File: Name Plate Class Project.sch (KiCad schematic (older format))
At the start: 0 parts

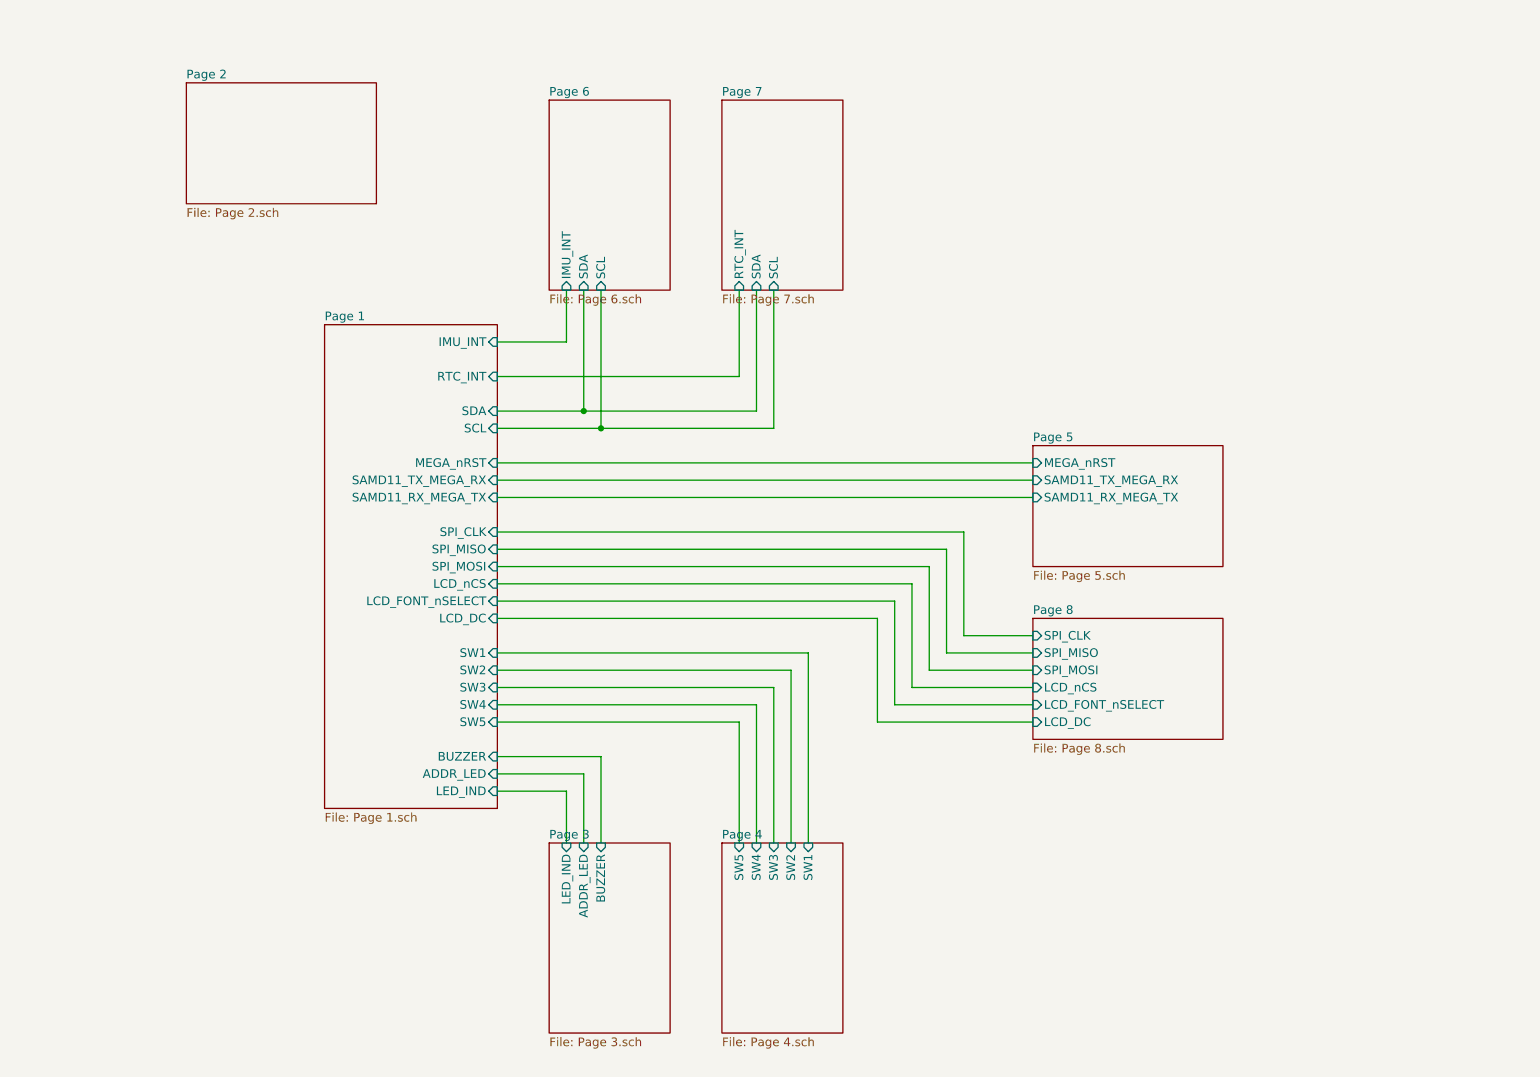
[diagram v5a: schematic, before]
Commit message: Updates to schematic
Switching to ATMega34UF chip.
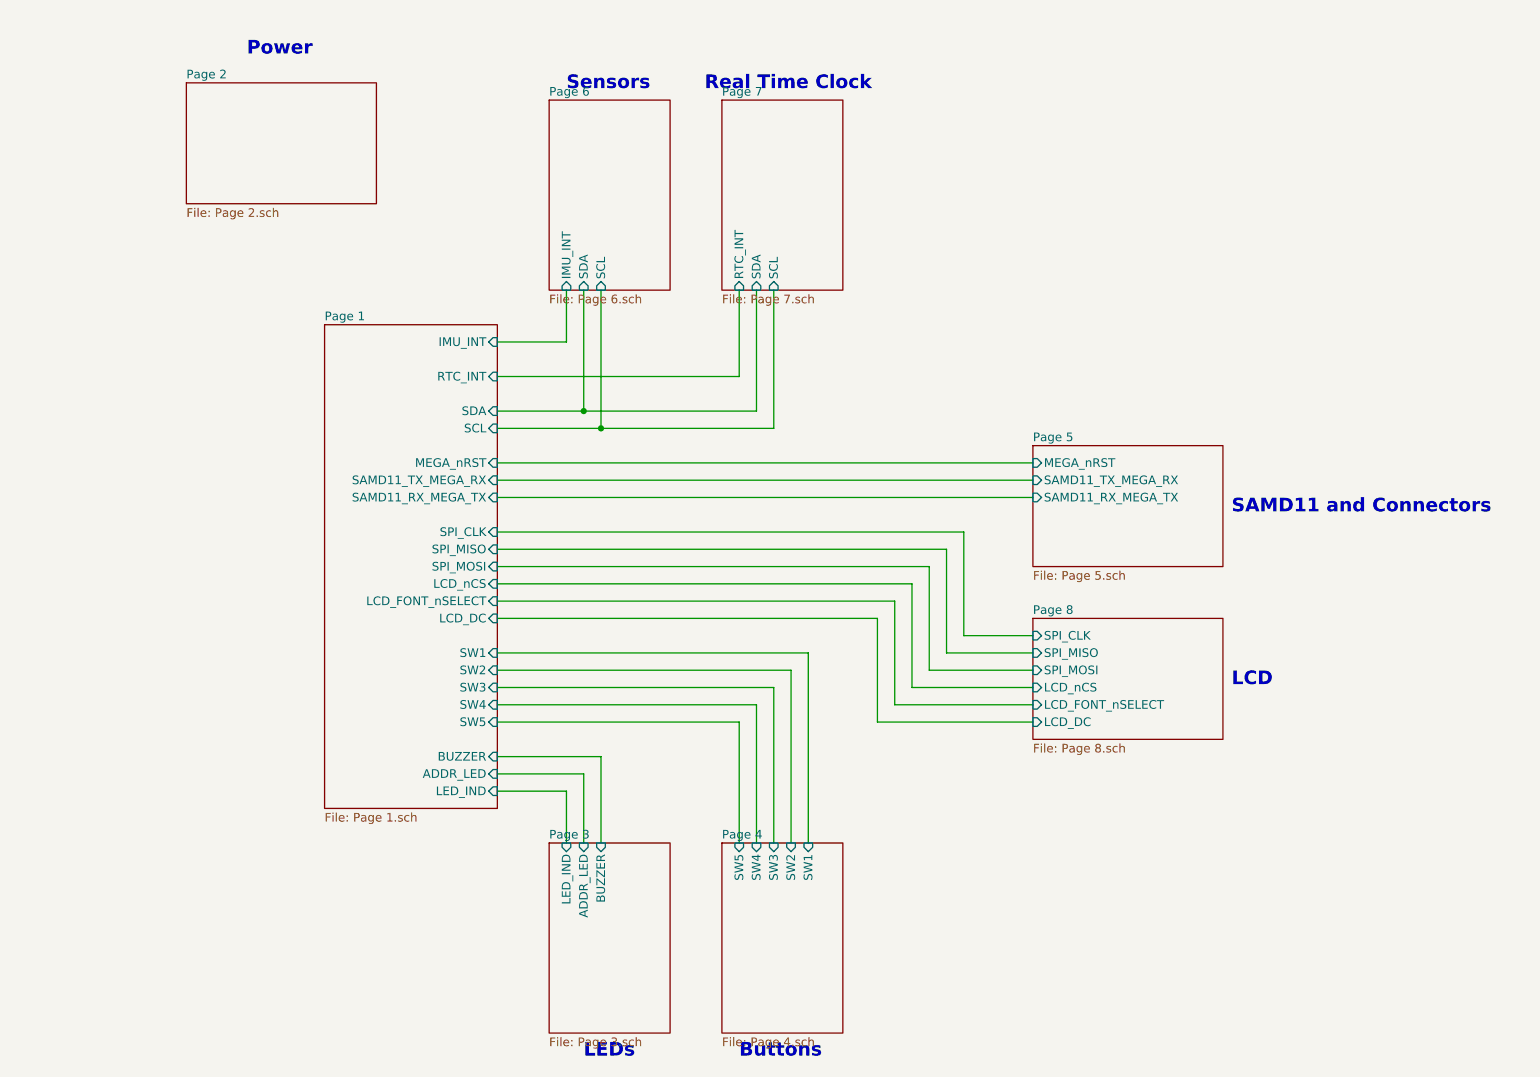
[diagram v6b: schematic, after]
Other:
- note added: "Buttons"
- note added: "LCD"
- note added: "LEDs"
- note added: "Power"
- note added: "Real Time Clock"
- note added: "SAMD11 and Connectors"
- note added: "Sensors"
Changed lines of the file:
@@
 F7 "LCD_nCS" I L 6900 4800 50
 $EndSheet
+Text Notes 8050 4800 0    79   ~ 16
+LCD
+Text Notes 8050 3800 0    79   ~ 16
+SAMD11 and Connectors
+Text Notes 5000 1350 0    79   ~ 16
+Real Time Clock
+Text Notes 4200 1350 0    79   ~ 16
+Sensors
+Text Notes 2350 1150 0    79   ~ 16
+Power
+Text Notes 4300 6950 0    79   ~ 16
+LEDs
+Text Notes 5200 6950 0    79   ~ 16
+Buttons
 $EndSCHEMATC
